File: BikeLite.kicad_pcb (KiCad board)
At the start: 2 copper layers, 51.8 x 34 mm, 22 parts, among them J1 Screw_Terminal_01x02, J2 Screw_Terminal_01x02, J3 Screw_Terminal_01x02, J4 Screw_Terminal_01x02, U1 LM2576HVT-ADJ, U2 NE555P

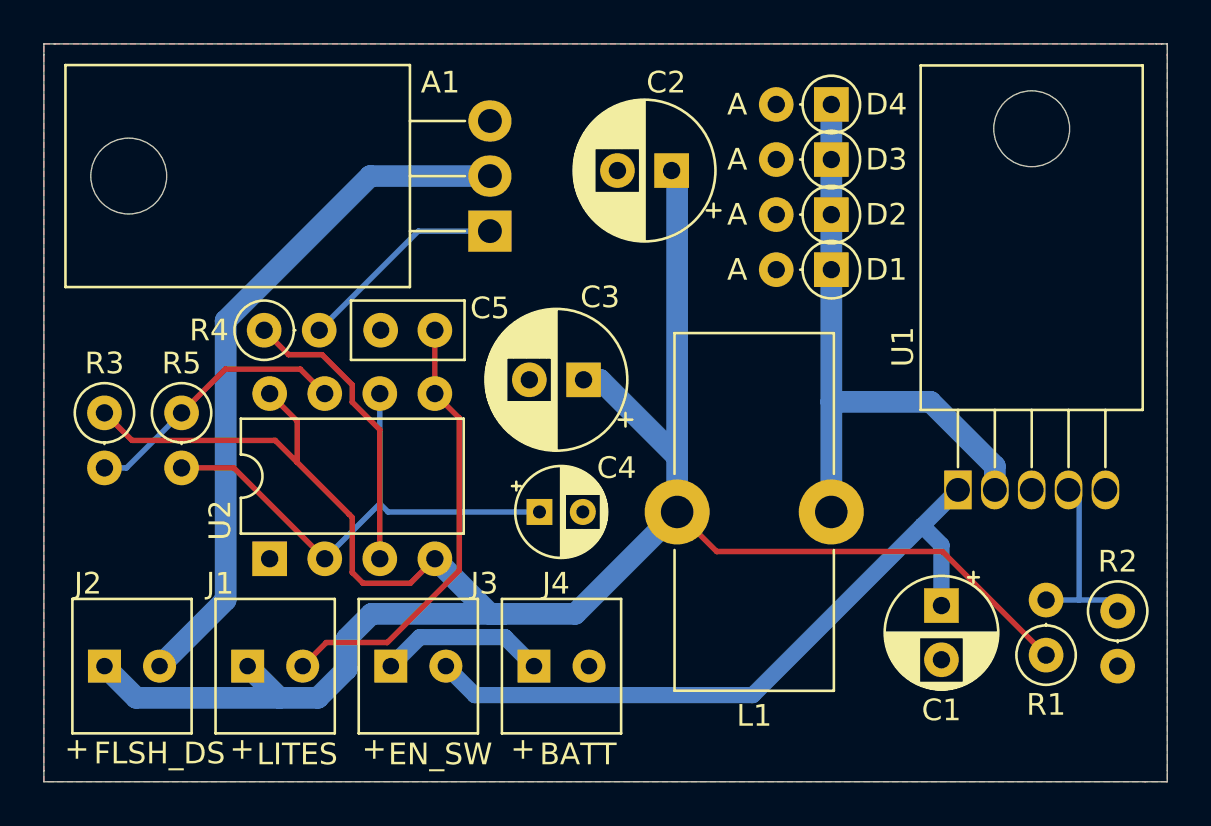
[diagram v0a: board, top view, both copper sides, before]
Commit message: Revision B
-Updated screw terminal dimensions and silkscreen labels
-Changed flash_disable signal to directly enable the MOSFET
-Updated inductor footprint dimensions
-Added schematic information on the silkscreen
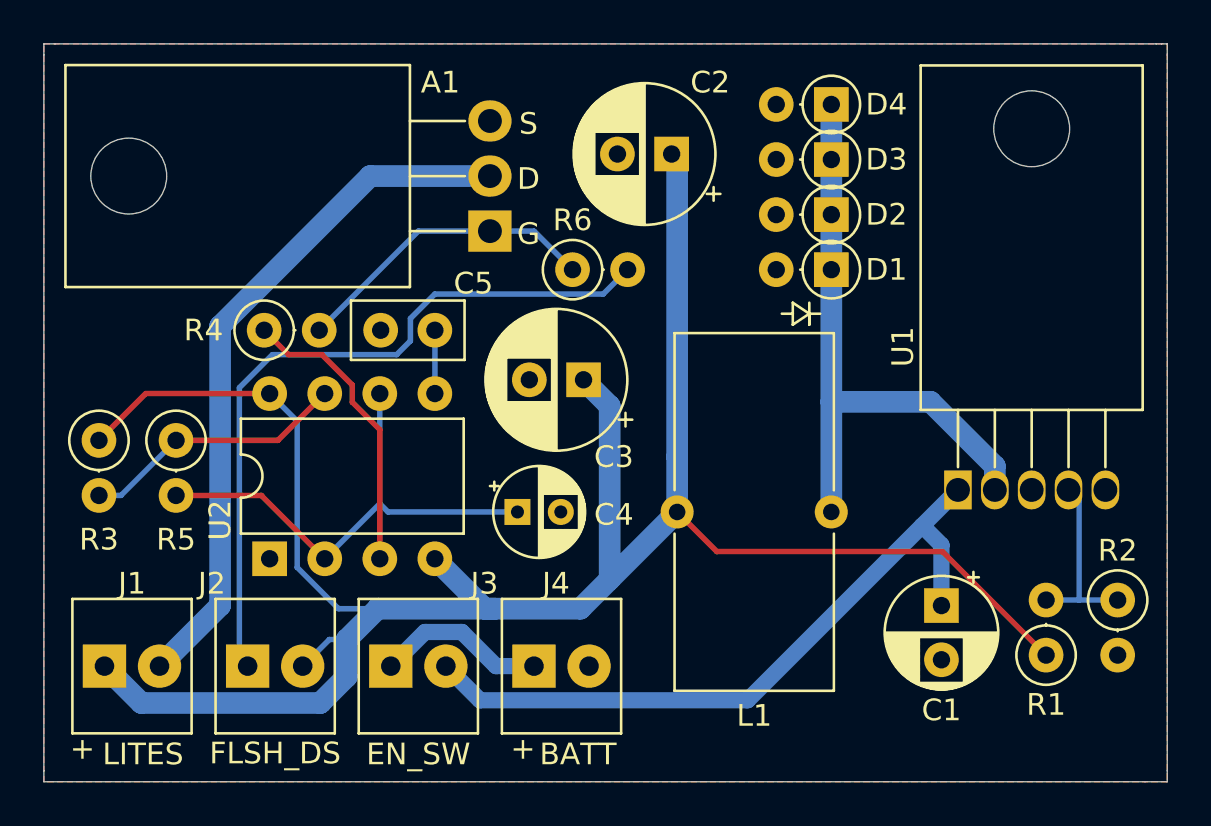
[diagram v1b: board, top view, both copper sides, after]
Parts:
- added R6: 10k, Resistor_THT:R_Axial_DIN0207_L6.3mm_D2.5mm_P2.54mm_Vertical, F.Cu at (150.4, 93.2)
- L1: footprint Inductor_THT:L_Toroid_Vertical_L16.3mm_W7.1mm_P7.11mm_Pulse_H -> BikeLite:L_Toroid_Vertical_L16.3mm_W7.1mm_P7.11mm_Pulse_H
- moved J1 6.60 mm to (130.0, 111.5)
- moved J2 6.60 mm to (136.7, 111.5)
- moved R3 1.30 mm to (128.5, 101.1)
- moved R5 1.30 mm to (132.1, 101.1)
- moved C4 1.02 mm to (147.8, 104.4)
- moved C2 0.76 mm to (154.9, 87.9)
- moved R2 0.51 mm to (175.5, 108.5)
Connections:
- net Net-(A1-Pad1) renamed LITE_EN
- C5 pad 1: FLSH_DSBL -> Net-(C5-Pad1)
- J1 pad 2: FLSH_DSBL -> LITE-
- J2 pad 1: V_out -> Net-(J2-Pad1)
- J2 pad 2: LITE- -> V_out
- U2 pad 5: FLSH_DSBL -> Net-(C5-Pad1)
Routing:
- net Net-(J2-Pad1): track 0.00 -> 33.8 mm
- net FLSH_DSBL: track 20.6 -> 0.00 mm
- net LITE_EN: track 9.77 -> 14.3 mm
- net V_out: track 103.2 -> 106.3 mm
- net Net-(C5-Pad1): track 0.00 -> 2.92 mm
- net Net-(C4-Pad1): track 24.5 -> 23.2 mm
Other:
- board text added: "Bike Lite - Rev B M. Frances 1/22"
- board text added: "C1 100uF C2 470uF C3 470uF C4 4.7uF C5 10nF L1 100uH"
- board text added: "D"
- board text added: "G"
- board text added: "LM2576-ADJ Buck Converter and Bistable 555 LED Driver"
- board text added: "R1 2.2k R2 680 R3 10k R4 10k R5 100k R6 10k"
- board text added: "S"
- board text added: "github.com/francesmatthew/BikeLite"
- board text removed: "Bike Lite - Rev A M. Frances 12/21"
